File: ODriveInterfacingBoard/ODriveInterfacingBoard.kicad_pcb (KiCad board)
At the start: 2 copper layers, 187.7 x 50 mm, 30 parts, among them U1 ODrive

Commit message: yee
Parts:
- Conn7: value M0_A -> ML
- Conn8: value M1_A -> MR
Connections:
- net L_Encoder_AO renamed L_Encoder_A
- net L_Encoder_BO renamed L_Encoder_B
- net L_Encoder_ZO renamed L_Encoder_Z
- net M0_A renamed ML_A
- net M0_B renamed ML_B
- net M0_C renamed ML_C
- net M1_A renamed MR_A
- net M1_B renamed MR_B
- net M1_C renamed MR_C
- net R_Encoder_AO renamed R_Encoder_A
- net R_Encoder_ZO renamed R_Encoder_Z
- Conn2 pad 3: GND -> R_Encoder_B
- Conn2 pad 5: GND -> R_Encoder_Gnd
- Conn3 pad 1: /PV+ -> GND
- Conn3 pad 4: GND -> /PV+
- U1 pad E1_B: GND -> R_Encoder_B
- U1 pad E1_GND: GND -> R_Encoder_Gnd
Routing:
- net GND: track 248.4 -> 21.8 mm, vias 138 -> 113
- net R_Encoder_B: track 0.00 -> 113.5 mm
- net R_Encoder_Gnd: track 0.00 -> 113.0 mm
- net /PV+: track 55.1 -> 58.3 mm
- net ML_B: track 60.5 -> 61.3 mm
- net ML_C: track 58.9 -> 59.4 mm
- net ML_A: track 86.0 -> 86.5 mm
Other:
- outline, holes or cut-outs redrawn
- board text added: "+"
- board text added: "-"
- board text added: "Z"

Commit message: Just need silks and vias, babam
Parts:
- added ?: , , F.Cu at (219.3, 111.8)
- added D16: Rx Yellow, LED_SMD:LED_0603_1608Metric_Pad1.05x0.95mm_HandSolder, F.Cu at (228.1, 100.1)
- added D17: Rx Yellow, LED_SMD:LED_0603_1608Metric_Pad1.05x0.95mm_HandSolder, F.Cu at (228.1, 106.4)
- added D18: Rx Yellow, LED_SMD:LED_0603_1608Metric_Pad1.05x0.95mm_HandSolder, F.Cu at (62.6, 103.1)
- added D19: Rx Yellow, LED_SMD:LED_0603_1608Metric_Pad1.05x0.95mm_HandSolder, F.Cu at (62.6, 99.9)
- added D20: Rx Yellow, LED_SMD:LED_0603_1608Metric_Pad1.05x0.95mm_HandSolder, F.Cu at (62.6, 106.3)
- added D4: Rx Yellow, LED_SMD:LED_0603_1608Metric_Pad1.05x0.95mm_HandSolder, F.Cu at (228.1, 103.3)
- added R11: 500, Resistor_SMD:R_0603_1608Metric_Pad1.05x0.95mm_HandSolder, F.Cu at (223.7, 106.4)
- added R12: 500, Resistor_SMD:R_0603_1608Metric_Pad1.05x0.95mm_HandSolder, F.Cu at (67.1, 103.1)
- added R13: 500, Resistor_SMD:R_0603_1608Metric_Pad1.05x0.95mm_HandSolder, F.Cu at (67.1, 99.9)
- added R14: 500, Resistor_SMD:R_0603_1608Metric_Pad1.05x0.95mm_HandSolder, F.Cu at (67.1, 106.3)
- added R4: 500, Resistor_SMD:R_0603_1608Metric_Pad1.05x0.95mm_HandSolder, F.Cu at (223.7, 103.3)
- added R5: 500, Resistor_SMD:R_0603_1608Metric_Pad1.05x0.95mm_HandSolder, F.Cu at (223.7, 100.1)
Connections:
- Conn1 pad 1: L_Encoder_5V -> GND
- Conn1 pad 2: L_Encoder_A -> L_Encoder_Z
- Conn1 pad 3: L_Encoder_B -> L_Encoder_A
- Conn1 pad 4: L_Encoder_Z -> L_Encoder_5V
- Conn1 pad 5: L_Encoder_Gnd -> L_Encoder_B
- Conn2 pad 1: R_Encoder_5V -> GND
- Conn2 pad 2: R_Encoder_A -> R_Encoder_Z
- Conn2 pad 3: R_Encoder_B -> R_Encoder_A
- Conn2 pad 4: R_Encoder_Z -> R_Encoder_5V
- Conn2 pad 5: R_Encoder_Gnd -> R_Encoder_B
- U1 pad E0_GND: L_Encoder_Gnd -> GND
- U1 pad E1_GND: R_Encoder_Gnd -> GND
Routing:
- net R_Encoder_Gnd: track 113.0 -> 0.00 mm
- net L_Encoder_Gnd: track 27.9 -> 0.00 mm
- net L_Encoder_B: track 32.4 -> 52.7 mm, vias 0 -> 1
- net R_Encoder_Z: track 112.8 -> 131.4 mm
- net L_Encoder_A: track 28.2 -> 44.8 mm, vias 0 -> 2
- net R_Encoder_B: track 113.5 -> 126.2 mm
- net R_Encoder_A: track 115.7 -> 127.3 mm, vias 0 -> 1
- net L_Encoder_5V: track 28.1 -> 38.0 mm, vias 0 -> 1
- net L_Encoder_Z: track 28.0 -> 35.3 mm, vias 0 -> 2
- net R_Encoder_5V: track 112.8 -> 105.6 mm
- net Net-(D20-Pad2): track 0.00 -> 2.71 mm
- net Net-(D19-Pad2): track 0.00 -> 2.70 mm
- net Net-(D18-Pad2): track 0.00 -> 2.70 mm
- net Net-(D4-Pad2): track 0.00 -> 2.69 mm
- net Net-(D17-Pad2): track 0.00 -> 2.69 mm
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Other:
- board text added: "Left Encoder"
- board text added: "Right Encoder"

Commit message: https://www.youtube.com/watch?v=dQw4w9WgXcQ
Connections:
- Conn9 pad 1: Tx -> Rx
- Conn9 pad 3: Rx -> Tx
- R1 pad 1: Tx -> Rx
- R2 pad 1: Rx -> Tx
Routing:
- net Rx: track 73.7 -> 74.1 mm, vias 2 -> 1
- net Tx: track 75.6 -> 75.9 mm, vias 1 -> 3
- net GND: vias 303 -> 344
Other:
- board text added: "If you can read this, Eli probably messed up"

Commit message: whoops this one
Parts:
- added G***: LOGO, SamacSys_Parts:Signature, F.Cu at (168.9, 104.8)
- added G***: LOGO, SamacSys_Parts:lizard_logo, F.Cu at (191.6, 95.6)
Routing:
- net GND: vias 344 -> 329
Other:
- board text added: "ODrive Breakout, Rev 1 Mars Rover, 2020 Missouri S&T Dan Napierkowski"

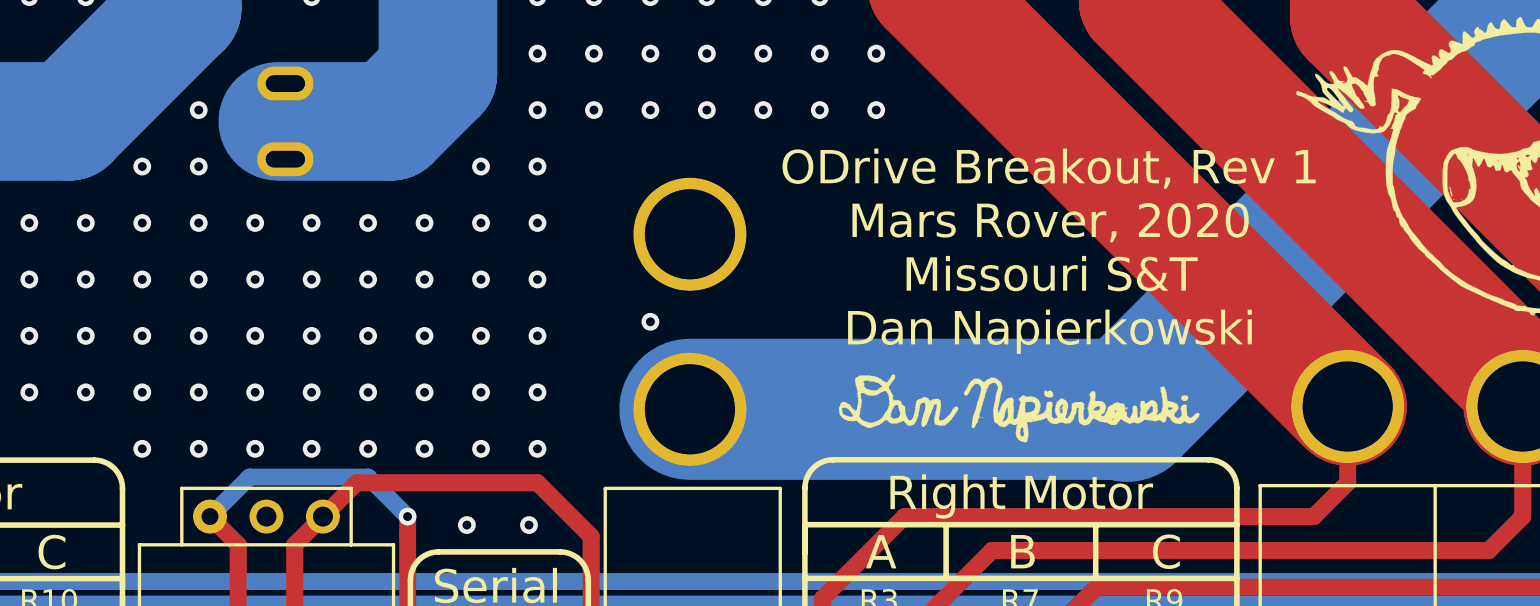
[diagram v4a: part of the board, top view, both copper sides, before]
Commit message: Fixed Silks, Changed rev number to 2
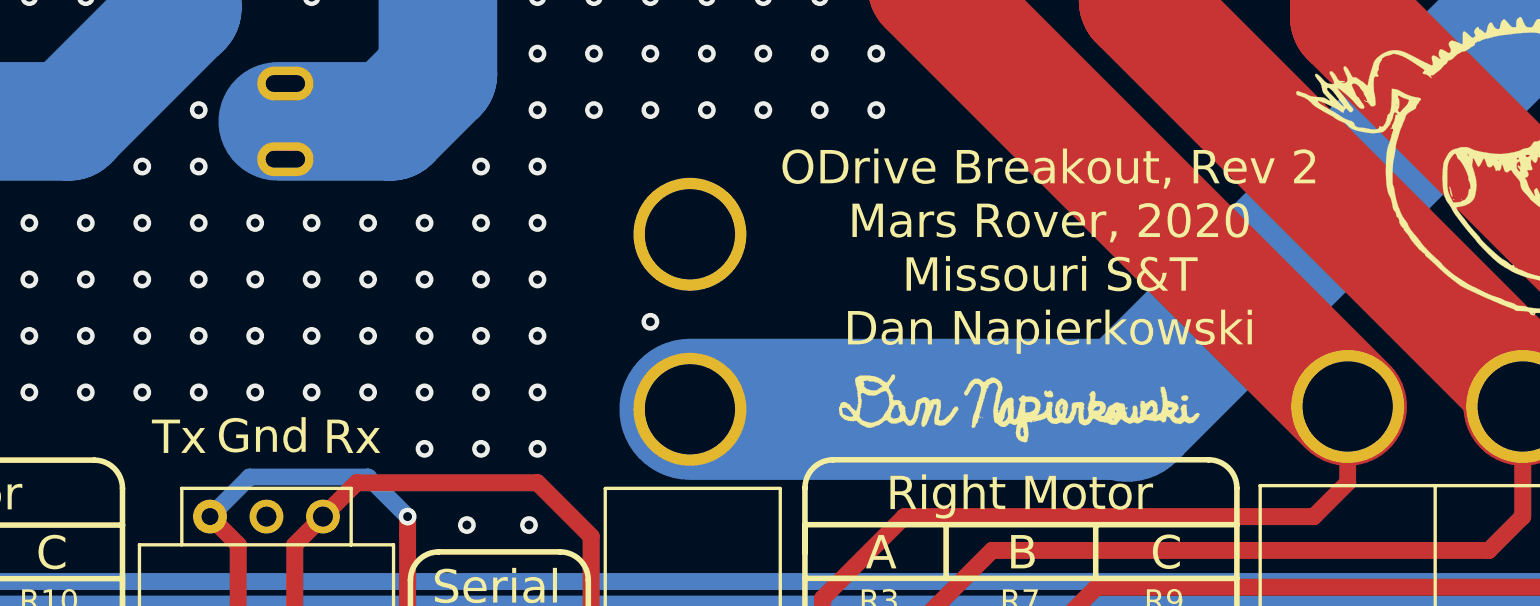
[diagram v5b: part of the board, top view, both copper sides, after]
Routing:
- net GND: vias 329 -> 324
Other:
- board text added: "Gnd"
- board text added: "ODrive Breakout, Rev 2 Mars Rover, 2020 Missouri S&T Dan Napierkowski"
- board text removed: "ODrive Breakout, Rev 1 Mars Rover, 2020 Missouri S&T Dan Napierkowski"
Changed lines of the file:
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@@
   (general
     (thickness 1.6)
-    (drawings 125)
-    (tracks 637)
+    (drawings 128)
+    (tracks 632)
     (zones 0)
     (modules 45)
@@
   (layers
     (0 F.Cu signal)
-    (31 B.Cu signal hide)
+    (31 B.Cu signal)
     (32 B.Adhes user)
     (33 F.Adhes user)
-    (34 B.Paste user hide)
-    (35 F.Paste user hide)
+    (34 B.Paste user)
+    (35 F.Paste user)
     (36 B.SilkS user)
     (37 F.SilkS user)
-    (38 B.Mask user hide)
-    (39 F.Mask user hide)
-    (40 Dwgs.User user hide)
+    (38 B.Mask user)
+    (39 F.Mask user)
+    (40 Dwgs.User user)
     (41 Cmts.User user)
     (42 Eco1.User user)
@@
     (47 F.CrtYd user)
     (48 B.Fab user)
-    (49 F.Fab user hide)
+    (49 F.Fab user)
   )
   (setup
-    (last_trace_width 6.35)
+    (last_trace_width 0.381)
     (user_trace_width 0.508)
     (user_trace_width 0.762)
@@
     )
   )
-  (gr_text "ODrive Breakout, Rev 1\nMars Rover, 2020\nMissouri S&T \nDan Napierkowski  \n" (at 170.3705 97.663) (layer F.SilkS)
+  (gr_text Rx (at 138.9888 106.172) (layer F.SilkS)
+    (effects (font (size 1.5 1.5) (thickness 0.25)))
+  )
+  (gr_text Tx (at 131.2164 106.172) (layer F.SilkS)
+    (effects (font (size 1.5 1.5) (thickness 0.25)))
+  )
+  (gr_text Gnd (at 134.9756 106.1212) (layer F.SilkS)
+    (effects (font (size 1.5 1.5) (thickness 0.25)))
+  )
+  (gr_text "ODrive Breakout, Rev 2\nMars Rover, 2020\nMissouri S&T \nDan Napierkowski  \n" (at 170.3705 97.663) (layer F.SilkS)
     (effects (font (size 1.5 1.5) (thickness 0.35)))
   )
@@
   (gr_arc (start 70.993 106.426) (end 70.993 107.696) (angle -90) (layer F.SilkS) (width 0.25))
   (gr_line (start 72.263 106.426) (end 72.263 97.028) (layer F.SilkS) (width 0.25))
-  (gr_text Z (at 211.6455 111.633) (layer B.SilkS)
+  (gr_text + (at 211.6455 111.633) (layer B.SilkS)
     (effects (font (size 1 1) (thickness 0.15)) (justify mirror))
   )
-  (gr_text + (at 219.3925 111.5695) (layer B.SilkS)
+  (gr_text - (at 219.3925 111.5695) (layer B.SilkS)
     (effects (font (size 1 1) (thickness 0.15)) (justify mirror))
   )
-  (gr_text - (at 209.1055 111.633) (layer B.SilkS)
+  (gr_text B (at 209.1055 111.633) (layer B.SilkS)
     (effects (font (size 1 1) (thickness 0.15)) (justify mirror))
   )
-  (gr_text A (at 216.789 111.633) (layer B.SilkS)
+  (gr_text Z (at 216.789 111.633) (layer B.SilkS)
     (effects (font (size 1 1) (thickness 0.15)) (justify mirror))
   )
-  (gr_text B (at 214.249 111.633) (layer B.SilkS)
+  (gr_text A (at 214.249 111.633) (layer B.SilkS)
     (effects (font (size 1 1) (thickness 0.15)) (justify mirror))
   )
-  (gr_text + (at 78.9305 111.5695) (layer B.SilkS)
+  (gr_text - (at 78.9305 111.5695) (layer B.SilkS)
     (effects (font (size 1 1) (thickness 0.15)) (justify mirror))
   )
-  (gr_text A (at 76.327 111.633) (layer B.SilkS)
+  (gr_text Z (at 76.327 111.633) (layer B.SilkS)
     (effects (font (size 1 1) (thickness 0.15)) (justify mirror))
   )
-  (gr_text B (at 73.787 111.633) (layer B.SilkS)
+  (gr_text A (at 73.787 111.633) (layer B.SilkS)
     (effects (font (size 1 1) (thickness 0.15)) (justify mirror))
   )
-  (gr_text Z (at 71.1835 111.633) (layer B.SilkS)
+  (gr_text + (at 71.1835 111.633) (layer B.SilkS)
     (effects (font (size 1 1) (thickness 0.15)) (justify mirror))
   )
-  (gr_text - (at 68.6435 111.633) (layer B.SilkS)
+  (gr_text B (at 68.6435 111.633) (layer B.SilkS)
     (effects (font (size 1 1) (thickness 0.15)) (justify mirror))
   )
@@
   (via (at 142.24 104.14) (size 0.8) (drill 0.4) (layers F.Cu B.Cu) (net 1))
   (via (at 142.24 106.68) (size 0.8) (drill 0.4) (layers F.Cu B.Cu) (net 1))
-  (via (at 139.7 106.68) (size 0.8) (drill 0.4) (layers F.Cu B.Cu) (net 1))
   (via (at 139.7 104.14) (size 0.8) (drill 0.4) (layers F.Cu B.Cu) (net 1))
   (via (at 139.7 101.6) (size 0.8) (drill 0.4) (layers F.Cu B.Cu) (net 1))
@@
   (via (at 137.16 101.6) (size 0.8) (drill 0.4) (layers F.Cu B.Cu) (net 1))
   (via (at 137.16 104.14) (size 0.8) (drill 0.4) (layers F.Cu B.Cu) (net 1))
-  (via (at 137.16 106.68) (size 0.8) (drill 0.4) (layers F.Cu B.Cu) (net 1))
-  (via (at 134.62 106.68) (size 0.8) (drill 0.4) (layers F.Cu B.Cu) (net 1))
   (via (at 134.62 104.14) (size 0.8) (drill 0.4) (layers F.Cu B.Cu) (net 1))
   (via (at 134.62 101.6) (size 0.8) (drill 0.4) (layers F.Cu B.Cu) (net 1))
@@
   (via (at 132.08 101.6) (size 0.8) (drill 0.4) (layers F.Cu B.Cu) (net 1))
   (via (at 132.08 104.14) (size 0.8) (drill 0.4) (layers F.Cu B.Cu) (net 1))
-  (via (at 132.08 106.68) (size 0.8) (drill 0.4) (layers F.Cu B.Cu) (net 1))
-  (via (at 129.54 106.68) (size 0.8) (drill 0.4) (layers F.Cu B.Cu) (net 1))
   (via (at 129.54 104.14) (size 0.8) (drill 0.4) (layers F.Cu B.Cu) (net 1))
   (via (at 129.54 101.6) (size 0.8) (drill 0.4) (layers F.Cu B.Cu) (net 1))

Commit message: added silks so they could feel like they did their job
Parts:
- added G***: LOGO, MRDT_Silkscreens:0_MRDT_Logo_20mm, B.Cu at (172.3, 93.1)
